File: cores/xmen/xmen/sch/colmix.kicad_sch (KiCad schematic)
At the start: 8 parts, among them J10 74LS157, J11 74LS157, J9 74LS157, K13 053251

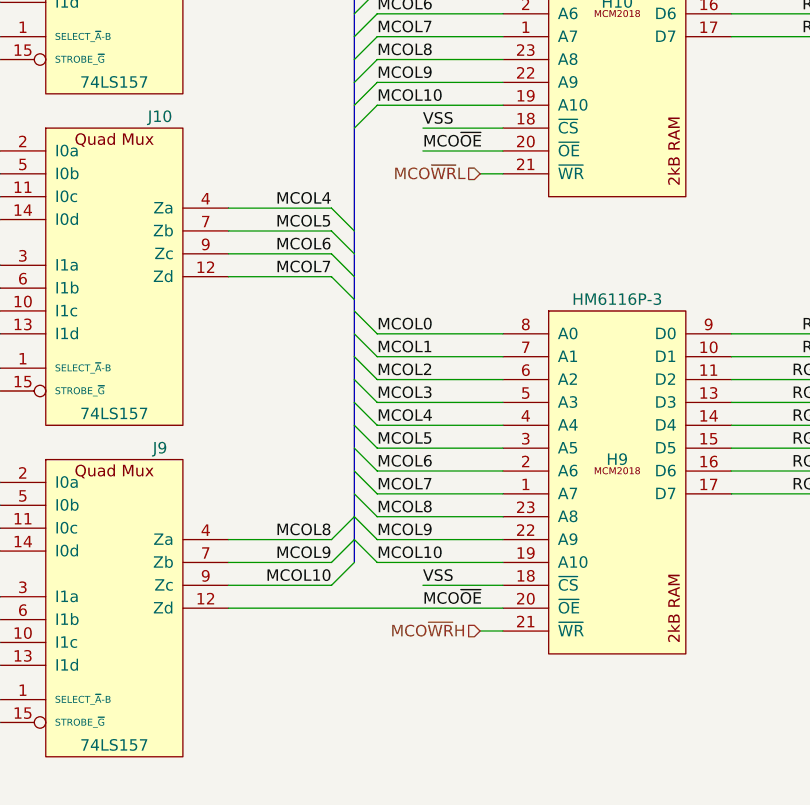
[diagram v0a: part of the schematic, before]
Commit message: Modification of signal names and pin order symbol 053246. Correction of MB8464
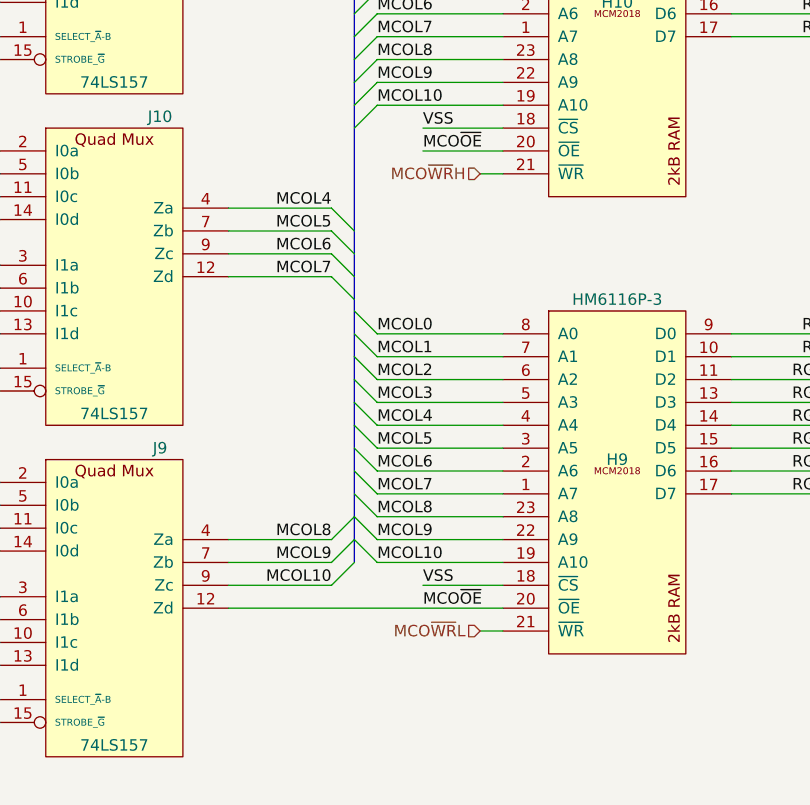
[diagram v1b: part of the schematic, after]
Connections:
- net MCO~{WR}H: now also H10.21 (~{WR}); no longer H9.21 (~{WR})
- net MCO~{WR}L: now also H9.21 (~{WR}); no longer H10.21 (~{WR})
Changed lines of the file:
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@@
     (effects (font (size 1.27 1.27)) (justify right))
   )
-  (hierarchical_label "MCO~{WR}L" (shape input) (at 313.69 121.92 180) (fields_autoplaced)
+  (hierarchical_label "MCO~{WR}H" (shape input) (at 313.69 121.92 180) (fields_autoplaced)
     (effects (font (size 1.27 1.27)) (justify right))
   )
-  (hierarchical_label "MCO~{WR}H" (shape input) (at 313.69 172.72 180) (fields_autoplaced)
+  (hierarchical_label "MCO~{WR}L" (shape input) (at 313.69 172.72 180) (fields_autoplaced)
     (effects (font (size 1.27 1.27)) (justify right))
   )
